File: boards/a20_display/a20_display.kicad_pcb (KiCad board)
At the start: 2 copper layers, 58.4 x 17.8 mm, 5 parts, among them P1 CONN_01X14

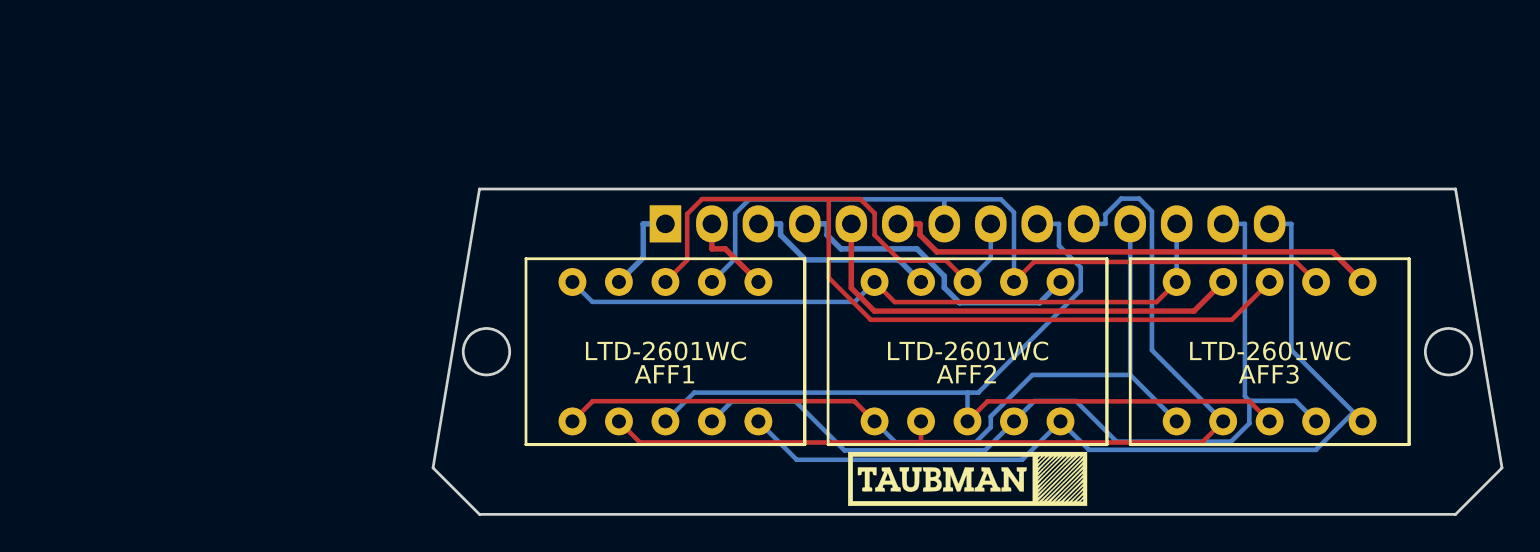
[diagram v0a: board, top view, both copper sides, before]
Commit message: Fix mounting holes and add back stripes.
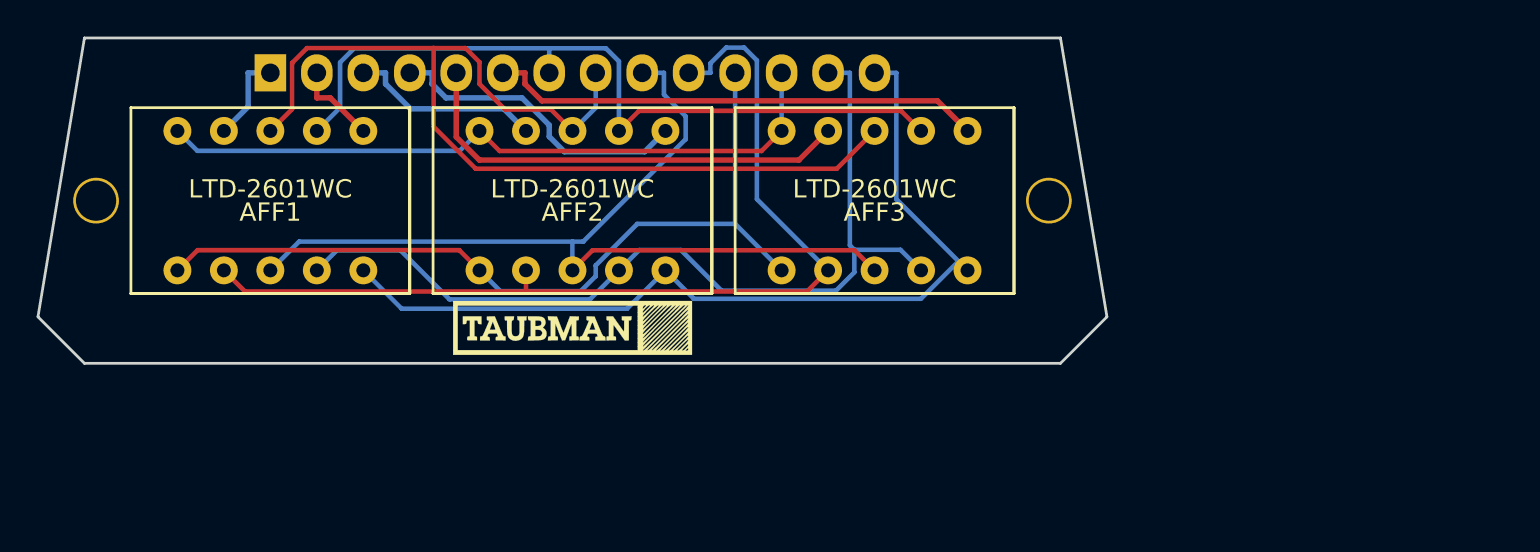
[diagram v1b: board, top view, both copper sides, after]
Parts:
- added G***: LOGO, te_logos:stripe_67mm, B.Cu at (137.8, 106.0)
- added REF**: 1pin, Connect:1pin, F.Cu at (164.5, 107.3)
- added REF**: 1pin, Connect:1pin, F.Cu at (112.4, 107.3)
- moved AFF2 23.1 mm to (138.4, 107.3)
- moved AFF3 23.1 mm to (154.9, 107.3)
- moved G*** 23.1 mm to (138.4, 114.2)
- moved AFF1 23.1 mm to (121.9, 107.3)
- moved P1 23.1 mm to (121.9, 100.3)
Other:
- outline, holes or cut-outs redrawn
